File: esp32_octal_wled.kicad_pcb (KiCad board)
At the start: 4 copper layers, 100 x 50 mm, 54 parts, among them J1 LED1, J11 I2C_Display, J12 ATX-24, J13 LED1, J14 LED1, J15 LED1, J16 LED1, J2 LED1, J3 PROG, J4 LED1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

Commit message: As ordered at JLCPCB
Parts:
- R2: value 10k -> 22k
- R3: value 10k -> 15k
- moved SW2 0.85 mm to (136.2, 71.8)
- moved C8 0.75 mm to (126.8, 69.9)
- moved R8 0.75 mm to (126.8, 71.9)
- moved SW4 0.35 mm to (123.2, 71.8)
- moved C9 0.35 mm to (113.8, 69.9)
- moved R12 0.30 mm to (113.9, 71.9)
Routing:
- net GND: track 44.9 -> 57.3 mm, vias 14 -> 118
- net +5V: track 112.7 -> 119.3 mm
- net SDA: track 67.7 -> 73.4 mm
- net 485_DE: track 23.8 -> 22.1 mm
- net Net-(J12-PWR_OK): track 35.9 -> 34.5 mm
- net Net-(R8-Pad1): track 8.54 -> 9.29 mm
- net +3V3: track 119.8 -> 119.3 mm, vias 28 -> 44
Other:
- board text added: "12V"
- board text added: "3V"
- board text added: "485A"
- board text added: "485B"
- board text added: "5V"
- board text added: "GND"
- board text added: "SCL"
- board text added: "SDA"

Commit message: Fixes
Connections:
- U2 pad 29: STRIP3 -> STRIP4
- U2 pad 30: STRIP4 -> STRIP3
- U2 pad 31: STRIP1 -> STRIP2
- U2 pad 33: STRIP2 -> STRIP1
- U3 pad 12: STRIP4 -> STRIP3
- U3 pad 2: STRIP1 -> STRIP2
- U3 pad 5: STRIP2 -> STRIP1
- U3 pad 9: STRIP3 -> STRIP4
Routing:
- net STRIP4: track 18.9 -> 12.7 mm
- net STRIP3: track 12.7 -> 18.9 mm
- net STRIP2: track 20.4 -> 21.4 mm
- net STRIP1: track 21.4 -> 20.4 mm
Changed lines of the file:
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@@
 			(layers "F.Cu" "F.Paste" "F.Mask")
 			(roundrect_rratio 0.25)
-			(net 29 "STRIP1")
+			(net 27 "STRIP2")
 			(pintype "input")
 		)
@@
 			(layers "F.Cu" "F.Paste" "F.Mask")
 			(roundrect_rratio 0.25)
-			(net 27 "STRIP2")
+			(net 29 "STRIP1")
 			(pintype "input")
 		)
@@
 			(layers "F.Cu" "F.Paste" "F.Mask")
 			(roundrect_rratio 0.25)
-			(net 28 "STRIP3")
+			(net 30 "STRIP4")
 			(pintype "input")
 		)
@@
 			(layers "F.Cu" "F.Paste" "F.Mask")
 			(roundrect_rratio 0.25)
-			(net 30 "STRIP4")
+			(net 28 "STRIP3")
 			(pintype "input")
 		)
@@
 			(layers "F.Cu" "F.Paste" "F.Mask")
 			(roundrect_rratio 0.25)
-			(net 28 "STRIP3")
+			(net 30 "STRIP4")
 			(pinfunction "GPIO5")
 			(pintype "bidirectional")
@@
 			(layers "F.Cu" "F.Paste" "F.Mask")
 			(roundrect_rratio 0.25)
-			(net 30 "STRIP4")
+			(net 28 "STRIP3")
 			(pinfunction "GPIO18")
 			(pintype "bidirectional")
@@
 			(layers "F.Cu" "F.Paste" "F.Mask")
 			(roundrect_rratio 0.25)
-			(net 29 "STRIP1")
+			(net 27 "STRIP2")
 			(pinfunction "GPIO19")
 			(pintype "bidirectional")
@@
 			(layers "F.Cu" "F.Paste" "F.Mask")
 			(roundrect_rratio 0.25)
-			(net 27 "STRIP2")
+			(net 29 "STRIP1")
 			(pinfunction "GPIO21")
 			(pintype "bidirectional")
@@
 	)
 	(segment
-		(start 61.812107 60)
-		(end 60.007106 60)
+		(start 77.04 58.224999)
+		(end 75.364999 59.9)
 		(width 0.3)
 		(layer "F.Cu")
@@
 	)
 	(segment
-		(start 62.412106 59.4)
-		(end 62.105 59.707106)
+		(start 75.364999 59.9)
+		(end 63.19 59.9)
 		(width 0.3)
 		(layer "F.Cu")
@@
 	)
 	(segment
-		(start 62.105 59.707107)
-		(end 61.812107 60)
+		(start 60.19 62.9)
+		(end 60.19 64.4)
 		(width 0.3)
 		(layer "F.Cu")
@@
 	)
 	(segment
-		(start 72.054999 59.4)
-		(end 62.412106 59.4)
+		(start 63.19 59.9)
+		(end 60.19 62.9)
 		(width 0.3)
 		(layer "F.Cu")
@@
 	)
 	(segment
-		(start 60.007106 60)
-		(end 57.65 62.357106)
+		(start 77.04 57.125)
+		(end 77.04 58.224999)
 		(width 0.3)
 		(layer "F.Cu")
@@
 	)
 	(segment
-		(start 62.105 59.707106)
-		(end 62.105 59.707107)
+		(start 75.938554 61.877893)
+		(end 75.938553 62.306447)
 		(width 0.3)
 		(layer "F.Cu")
-		(net 27)
+		(net 28)
 	)
 	(segment
-		(start 73.23 58.224999)
-		(end 72.054999 59.4)
+		(start 63.5 60.4)
+		(end 61.46 62.44)
 		(width 0.3)
 		(layer "F.Cu")
-		(net 27)
+		(net 28)
 	)
 	(segment
-		(start 73.23 57.125)
-		(end 73.23 58.224999)
+		(start 75.77 62.475)
+		(end 75.77 61.709339)
 		(width 0.3)
 		(layer "F.Cu")
-		(net 27)
+		(net 28)
 	)
 	(segment
-		(start 57.65 62.357106)
-		(end 57.65 64.4)
+		(start 61.46 62.44)
+		(end 61.46 64.4)
 		(width 0.3)
 		(layer "F.Cu")
-		(net 27)
+		(net 28)
 	)
 	(segment
-		(start 72.128554 62.102292)
-		(end 70.926262 60.9)
+		(start 74.460661 60.4)
+		(end 63.5 60.4)
 		(width 0.3)
 		(layer "F.Cu")
@@
 	)
 	(segment
-		(start 70.926262 60.9)
-		(end 64.240592 60.9)
+		(start 75.77 61.709339)
+		(end 74.460661 60.4)
 		(width 0.3)
 		(layer "F.Cu")
@@
 	)
 	(segment
-		(start 62.73 62.410592)
-		(end 62.73 64.4)
+		(start 61.812107 60)
+		(end 60.007106 60)
 		(width 0.3)
 		(layer "F.Cu")
-		(net 28)
+		(net 29)
 	)
 	(segment
-		(start 72.128553 62.306447)
-		(end 72.128554 62.102292)
+		(start 62.412106 59.4)
+		(end 62.105 59.707106)
 		(width 0.3)
 		(layer "F.Cu")
-		(net 28)
+		(net 29)
 	)
 	(segment
-		(start 64.240592 60.9)
-		(end 62.73 62.410592)
+		(start 62.105 59.707107)
+		(end 61.812107 60)
 		(width 0.3)
 		(layer "F.Cu")
-		(net 28)
+		(net 29)
 	)
 	(segment
-		(start 77.04 58.224999)
-		(end 75.364999 59.9)
+		(start 72.054999 59.4)
+		(end 62.412106 59.4)
 		(width 0.3)
 		(layer "F.Cu")
@@
 	)
 	(segment
-		(start 75.364999 59.9)
-		(end 63.19 59.9)
+		(start 60.007106 60)
+		(end 57.65 62.357106)
 		(width 0.3)
 		(layer "F.Cu")
@@
 	)
 	(segment
-		(start 60.19 62.9)
-		(end 60.19 64.4)
+		(start 62.105 59.707106)
+		(end 62.105 59.707107)
 		(width 0.3)
 		(layer "F.Cu")
@@
 	)
 	(segment
-		(start 63.19 59.9)
-		(end 60.19 62.9)
+		(start 73.23 58.224999)
+		(end 72.054999 59.4)
 		(width 0.3)
 		(layer "F.Cu")
@@
 	)
 	(segment
-		(start 77.04 57.125)
-		(end 77.04 58.224999)
+		(start 73.23 57.125)
+		(end 73.23 58.224999)
 		(width 0.3)
 		(layer "F.Cu")
@@
 	)
 	(segment
-		(start 75.938554 61.877893)
-		(end 75.938553 62.306447)
+		(start 57.65 62.357106)
+		(end 57.65 64.4)
 		(width 0.3)
 		(layer "F.Cu")
-		(net 30)
+		(net 29)
 	)
 	(segment
-		(start 63.5 60.4)
-		(end 61.46 62.44)
+		(start 72.128554 62.102292)
+		(end 70.926262 60.9)
 		(width 0.3)
 		(layer "F.Cu")
@@
 	)
 	(segment
-		(start 75.77 62.475)
-		(end 75.77 61.709339)
+		(start 70.926262 60.9)
+		(end 64.240592 60.9)
 		(width 0.3)
 		(layer "F.Cu")
@@
 	)
 	(segment
-		(start 61.46 62.44)
-		(end 61.46 64.4)
+		(start 62.73 62.410592)
+		(end 62.73 64.4)
 		(width 0.3)
 		(layer "F.Cu")
@@
 	)
 	(segment
-		(start 74.460661 60.4)
-		(end 63.5 60.4)
+		(start 72.128553 62.306447)
+		(end 72.128554 62.102292)
 		(width 0.3)
 		(layer "F.Cu")
@@
 	)
 	(segment
-		(start 75.77 61.709339)
-		(end 74.460661 60.4)
+		(start 64.240592 60.9)
+		(end 62.73 62.410592)
 		(width 0.3)
 		(layer "F.Cu")

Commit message: INMP441
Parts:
- added F1: 2A, Fuse:Fuse_2920_7451Metric_Pad2.10x5.45mm_HandSolder, B.Cu at (58.0, 48.1)
- added F2: 2A, Fuse:Fuse_2920_7451Metric_Pad2.10x5.45mm_HandSolder, B.Cu at (70.0, 48.1)
- added F3: 2A, Fuse:Fuse_2920_7451Metric_Pad2.10x5.45mm_HandSolder, B.Cu at (82.0, 48.1)
- added F4: 2A, Fuse:Fuse_2920_7451Metric_Pad2.10x5.45mm_HandSolder, B.Cu at (94.0, 48.1)
- added F5: 2A, Fuse:Fuse_2920_7451Metric_Pad2.10x5.45mm_HandSolder, B.Cu at (106.0, 48.1)
- added F6: 2A, Fuse:Fuse_2920_7451Metric_Pad2.10x5.45mm_HandSolder, B.Cu at (118.0, 48.1)
- added F7: 2A, Fuse:Fuse_2920_7451Metric_Pad2.10x5.45mm_HandSolder, B.Cu at (130.1, 48.1)
- added F8: 2A, Fuse:Fuse_2920_7451Metric_Pad2.10x5.45mm_HandSolder, B.Cu at (142.0, 48.1)
- added J10: EXT2, Connector_JST:JST_XH_B5B-XH-A_1x05_P2.50mm_Vertical, F.Cu at (147.5, 76.7)
- added J9: TXRX, TestPoint:TestPoint_2Pads_Pitch2.54mm_Drill0.8mm, F.Cu at (68.8, 57.9)
- added U6: INMP441_Module, liebler_MODULES:INMP441_Module, F.Cu at (62.6, 86.4)
- J3: footprint liebler_CONN:IDC_2x03_P1.27mm_Vertical -> Connector:Tag-Connect_TC2030-IDC-NL_2x03_P1.27mm_Vertical
- moved R2 3.52 mm to (61.7, 86.9)
- moved R3 3.47 mm to (61.7, 85.0)
- moved R4 2.05 mm to (69.3, 83.6), turned to -90 degrees
- moved R11 1.71 mm to (66.5, 55.8), turned to 0 degrees
- moved C6 1.60 mm to (52.0, 83.3)
- moved C7 1.60 mm to (52.0, 85.3)
- moved U2 1.60 mm to (59.5, 71.8)
- moved R7 1.38 mm to (54.9, 84.5)
- moved C11 1.12 mm to (80.3, 60.7)
- moved J3 1.05 mm to (61.1, 56.6), turned to 0 degrees
- moved U3 0.40 mm to (74.7, 59.5)
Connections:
- J1 pad 1: +12V -> Net-(J1-Pin_1)
- J13 pad 1: +12V -> Net-(J13-Pin_1)
- J14 pad 1: +12V -> Net-(J14-Pin_1)
- J15 pad 1: +12V -> Net-(J15-Pin_1)
- J16 pad 1: +12V -> Net-(J16-Pin_1)
- J2 pad 1: +12V -> Net-(J2-Pin_1)
- J6 pad 1: +12V -> Net-(J6-Pin_1)
- J7 pad 1: +12V -> Net-(J7-Pin_1)
- U2 pad 4: unconnected-(U2-SENSOR_VP/GPIO36/ADC1_CH0-Pad4) -> THERM
- U2 pad 6: PWR_OK -> I2S_SD
- U2 pad 7: THERM -> PWR_OK
- U2 pad 8: unconnected-(U2-32K_XP/GPIO32/ADC1_CH4-Pad8) -> I2S_WS
- U2 pad 9: unconnected-(U2-32K_XN/GPIO33/ADC1_CH5-Pad9) -> I2S_SCK
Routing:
- net +3V3: track 119.3 -> 220.1 mm, vias 44 -> 45
- net SCL2: track 10.4 -> 102.5 mm
- net SDA2: track 11.0 -> 101.2 mm
- net +5V: track 119.3 -> 155.4 mm
- net I2S_WS: track 0.00 -> 9.47 mm
- net PROG_TX: track 10.1 -> 18.6 mm, vias 0 -> 1
- net I2S_SCK: track 0.00 -> 7.15 mm
- net THERM: track 74.3 -> 80.2 mm
- net Net-(J2-Pin_1): track 0.00 -> 5.01 mm
- net Net-(J15-Pin_1): track 0.00 -> 4.93 mm
- net Net-(J7-Pin_1): track 0.00 -> 4.91 mm
- net Net-(J6-Pin_1): track 0.00 -> 4.91 mm
- net Net-(J16-Pin_1): track 0.00 -> 4.91 mm
- net Net-(J14-Pin_1): track 0.00 -> 4.91 mm
- net Net-(J13-Pin_1): track 0.00 -> 4.91 mm
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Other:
- board text added: "RXTX"
- board text removed: "RS485"

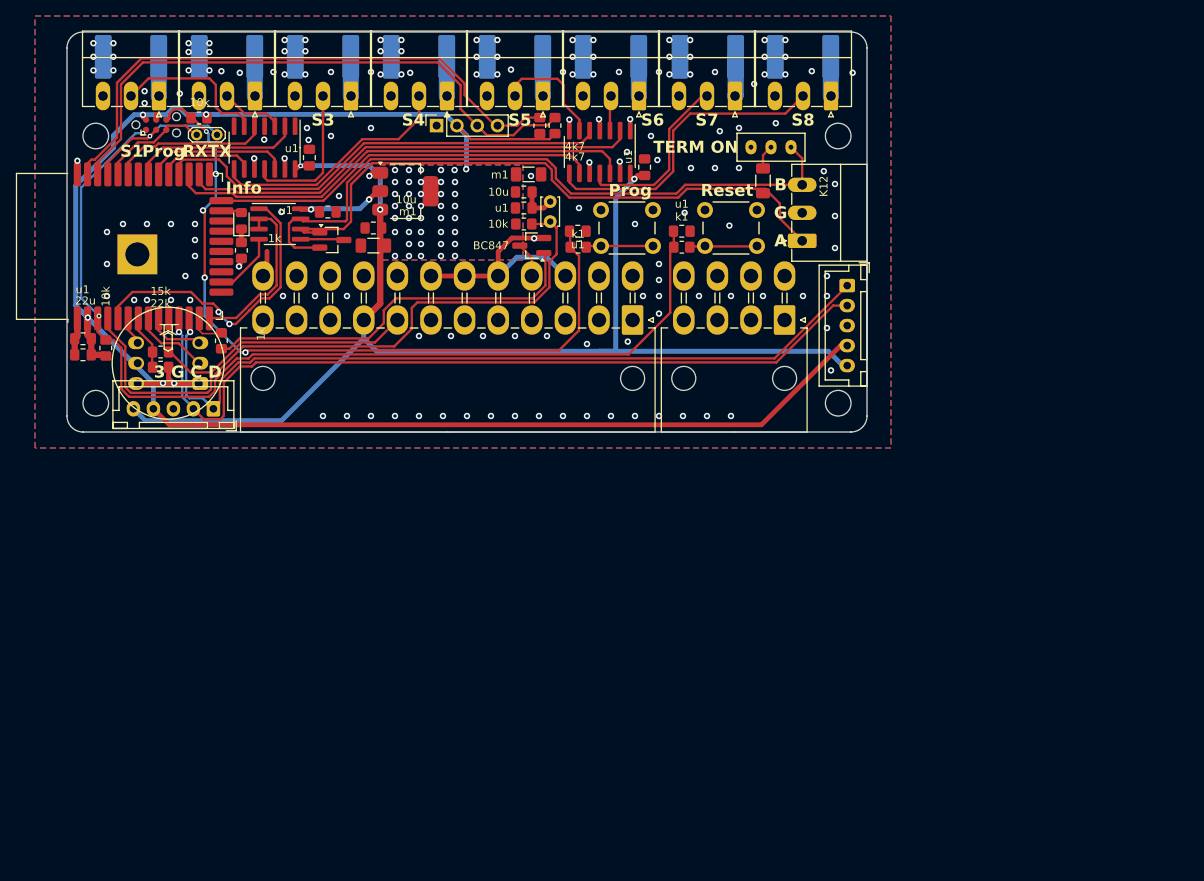
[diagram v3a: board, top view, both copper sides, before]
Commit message: Two layer PCB, other PCB format
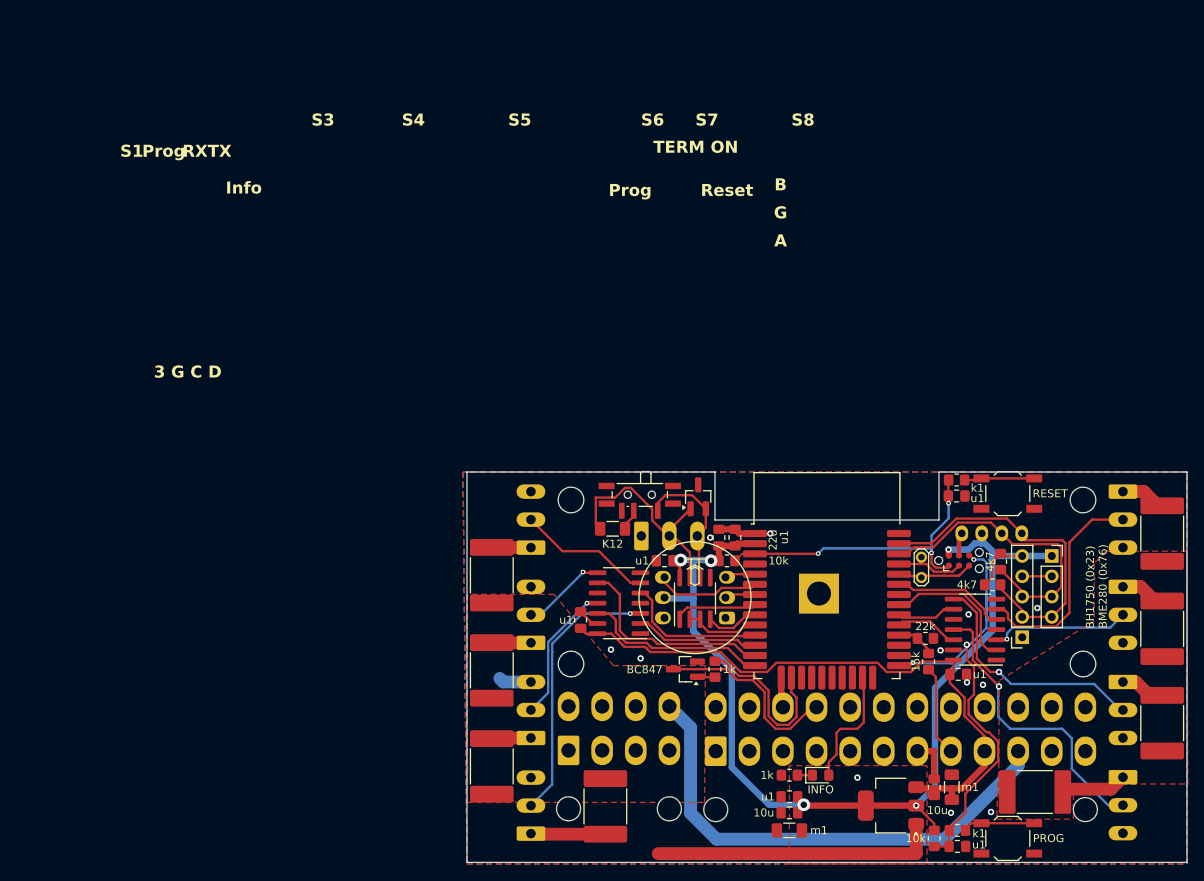
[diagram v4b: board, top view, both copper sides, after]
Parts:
- removed J10, J5: EXT2, Connector_JST:JST_XH_B5B-XH-A_1x05_P2.50mm_Vertical
- removed R13: 10k, Resistor_SMD:R_0805_2012Metric_Pad1.20x1.40mm_HandSolder
- removed TH1: NTC, Capacitor_THT:C_Disc_D3.4mm_W2.1mm_P2.50mm
- added J17: BH1750 (0x23), Connector_PinSocket_2.54mm:PinSocket_1x05_P2.54mm_Vertical, F.Cu at (169.4, 120.7)
- added J18: BME280 (0x76), Connector_PinSocket_2.54mm:PinSocket_1x04_P2.54mm_Vertical, F.Cu at (173.1, 110.5)
- F1, F2, F3, F4, F5, F6, F7, F8: moved to F.Cu
- J1, J12, J13, J14, J15, J16, J2, J4, J6, J7, J8: moved to B.Cu
- J11: value I2C_Display -> I2C EXT; footprint Connector_PinSocket_2.54mm:PinSocket_1x04_P2.54mm_Vertical -> liebler_CONN:JST_XH_S4B-XH-A-1_1x04_P2.50mm_Horizontal_SmallerCourtyard; moved to B.Cu
- SW1: footprint liebler_MECH:Switch_SS12D00 -> liebler_MECH:SW_SPDT_PCM12_handsolder
- SW2, SW4: footprint Button_Switch_THT:SW_PUSH_6mm_H13mm -> liebler_MECH:SW_SPST_TL3342_smaller_handsolder
- moved R11 128.7 mm to (158.4, 145.8), turned to 90 degrees
- moved J3 114.2 mm to (161.5, 111.1)
- moved F1 110.9 mm to (117.3, 141.8), turned to -90 degrees
- moved C11 103.7 mm to (161.4, 125.3), turned to 0 degrees
- moved R3 103.5 mm to (157.7, 123.7), turned to -90 degrees
- moved J9 102.7 mm to (156.8, 110.7), turned to -90 degrees
- moved J1 101.8 mm to (108.0, 141.7), turned to 90 degrees
- moved R2 101.4 mm to (157.3, 120.8)
- moved F7 100.8 mm to (186.9, 131.4), turned to 90 degrees
- moved F5 100.5 mm to (186.9, 107.7), turned to 90 degrees
- moved D2 100.2 mm to (144.2, 137.9), turned to 0 degrees
- moved F6 99.3 mm to (186.9, 119.6), turned to 90 degrees
- moved C1 99.0 mm to (160.6, 139.4), turned to 90 degrees
- moved C2 99.0 mm to (158.4, 139.4), turned to 90 degrees
- moved U1 97.9 mm to (153.0, 141.7), turned to 180 degrees
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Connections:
- D1 pad 1: RS485A -> RS485B
- D1 pad 2: RS485B -> RS485A
- J4 pad 1: RS485A -> GND
- J4 pad 2: GND -> RS485B
- J4 pad 3: RS485B -> RS485A
- R1 pad 1: RS485A -> RS485B
- SW1 pad 1: RS485B -> RS485A
- U2 pad 10: unconnected-(U2-DAC_1/ADC2_CH8/GPIO25-Pad10) -> 485_DE
- U2 pad 11: SCL2 -> STRIP4
- U2 pad 12: SDA2 -> STRIP1
- U2 pad 13: K1 -> STRIP3
- U2 pad 14: 485_DE -> STRIP2
- U2 pad 16: 485_DI -> K1
- U2 pad 24: STRIP8 -> unconnected-(U2-ADC2_CH2/GPIO2-Pad24)
- U2 pad 26: STRIP6 -> unconnected-(U2-ADC2_CH0/GPIO4-Pad26)
- U2 pad 27: STRIP7 -> unconnected-(U2-GPIO16-Pad27)
- U2 pad 28: STRIP5 -> PWR_OK
- U2 pad 29: STRIP4 -> STRIP8
- U2 pad 30: STRIP3 -> STRIP7
- U2 pad 31: STRIP2 -> STRIP6
- U2 pad 33: STRIP1 -> STRIP5
- U2 pad 5: 485_RO -> I2S_SCK
- U2 pad 7: PWR_OK -> I2S_WS
- U2 pad 8: I2S_WS -> 485_RO
- U2 pad 9: I2S_SCK -> 485_DI
- U3 pad 11: STRIP_5V_3 -> STRIP_5V_2
- U3 pad 12: STRIP3 -> STRIP2
- U3 pad 2: STRIP2 -> STRIP1
- U3 pad 3: STRIP_5V_2 -> STRIP_5V_1
- U3 pad 5: STRIP1 -> STRIP4
- U3 pad 6: STRIP_5V_1 -> STRIP_5V_4
- U3 pad 8: STRIP_5V_4 -> STRIP_5V_3
- U3 pad 9: STRIP4 -> STRIP3
- U4 pad 11: STRIP_5V_7 -> STRIP_5V_8
- U4 pad 12: STRIP7 -> STRIP8
- U4 pad 8: STRIP_5V_8 -> STRIP_5V_7
- U4 pad 9: STRIP8 -> STRIP7
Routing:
- net SCL2: track 102.5 -> 0.00 mm, vias 1 -> 0
- net SDA2: track 101.2 -> 0.00 mm, vias 1 -> 0
- net +3V3: track 220.1 -> 136.3 mm, vias 45 -> 5
- net PROG_EN: track 123.2 -> 39.6 mm, vias 2 -> 3
- net THERM: track 80.2 -> 0.00 mm
- net +5V: track 155.4 -> 77.7 mm, vias 3 -> 0
- net +12V: track 0.00 -> 62.4 mm, vias 48 -> 0
- net RS485A: track 78.2 -> 17.3 mm
- net RS485B: track 84.3 -> 28.2 mm
- net STRIP7: track 59.2 -> 7.41 mm
- net Net-(Q2-B): track 48.6 -> 2.22 mm
- net STRIP5: track 56.5 -> 14.3 mm
- net STRIP8: track 48.7 -> 7.94 mm
- net STRIP6: track 57.0 -> 17.9 mm
- net SCL: track 74.3 -> 38.0 mm
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- added copper zone on F.Cu, net +12V
- removed copper zone on In1.Cu, net +12V
- removed copper zone on B.Cu, net +3V3
- removed copper zone on In2.Cu, net GND
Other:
- board size 100 x 50 mm -> 90 x 48.8 mm
- copper layers 4 -> 2

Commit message: Various
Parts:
- added C13: u1, Capacitor_SMD:C_0805_2012Metric_Pad1.18x1.45mm_HandSolder, F.Cu at (160.0, 118.5)
- added J5: CAN, Connector_Phoenix_MC:PhoenixContact_MCV_1,5_2-G-3.5_1x02_P3.50mm_Vertical, B.Cu at (167.7, 121.3)
- added R10: 10k, Resistor_SMD:R_0805_2012Metric_Pad1.20x1.40mm_HandSolder, F.Cu at (166.3, 118.5)
- added R14: 1k, Resistor_SMD:R_0805_2012Metric_Pad1.20x1.40mm_HandSolder, F.Cu at (123.8, 123.7)
- added U10: SR602, liebler_MODULES:PIR_Sensor_SR602, B.Cu at (113.6, 113.5)
- added U7: SN65HVD230, liebler_SEMICONDUCTORS:SOIC-8_3.9x4.9mm_P1.27mm_handsolder, F.Cu at (161.8, 123.2)
- added U9: DS18B20, Package_TO_SOT_THT:TO-92L_HandSolder, B.Cu at (119.8, 123.8)
- J17, J18, U6: moved to B.Cu
- J4: value LED1 -> RS485
- moved R1 14.4 mm to (104.5, 102.7), turned to 90 degrees
- moved J17 13.3 mm to (157.1, 115.7)
- moved U4 11.5 mm to (174.0, 114.9)
- moved C11 10.3 mm to (169.2, 118.5), turned to 90 degrees
- moved R3 8.28 mm to (164.1, 118.5)
- moved C9 7.20 mm to (164.3, 140.2)
- moved U3 7.11 mm to (113.8, 111.5)
- moved R9 6.50 mm to (146.8, 137.8)
- moved J18 6.36 mm to (168.3, 114.7), turned to 90 degrees
- moved D2 6.30 mm to (150.5, 137.8)
- moved C2 6.01 mm to (164.3, 138.2), turned to 0 degrees
- moved R11 5.64 mm to (163.3, 143.1)
- moved R2 5.21 mm to (161.9, 118.5), turned to 90 degrees
- moved U1 5.14 mm to (158.0, 142.9)
- moved R5 4.44 mm to (167.0, 109.8)
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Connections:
- J11 pad 1: GND -> +3V3
- J11 pad 2: +3V3 -> GND
- J4 pad 2: RS485B -> RS485A
- J4 pad 3: RS485A -> RS485B
- SW1 pad CASE: (no net) -> GND
- U2 pad 10: 485_DE -> 485_DI
- U2 pad 16: K1 -> Onewire
- U2 pad 24: unconnected-(U2-ADC2_CH2/GPIO2-Pad24) -> K1
- U2 pad 26: unconnected-(U2-ADC2_CH0/GPIO4-Pad26) -> CAN_RX
- U2 pad 27: unconnected-(U2-GPIO16-Pad27) -> CAN_TX
- U2 pad 4: THERM -> MOVE
- U2 pad 5: I2S_SCK -> I2S_SD
- U2 pad 6: I2S_SD -> 485_RO
- U2 pad 8: 485_RO -> 485_DE
- U2 pad 9: 485_DI -> I2S_SCK
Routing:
- net GND: track 63.4 -> 143.0 mm, vias 12 -> 117
- net +5V: track 77.7 -> 127.5 mm, vias 0 -> 1
- net Onewire: track 0.00 -> 24.5 mm
- net MOVE: track 0.00 -> 19.3 mm
- net STRIP_5V_5: track 27.8 -> 9.26 mm
- net Net-(SW1-B): track 2.70 -> 20.1 mm
- net PWR_OK: track 4.95 -> 18.8 mm, vias 0 -> 2
- net STRIP7: track 7.41 -> 20.9 mm
- net STRIP6: track 17.9 -> 31.4 mm
- net STRIP5: track 14.3 -> 26.1 mm
- net STRIP8: track 7.94 -> 19.5 mm
- net STRIP_5V_6: track 17.5 -> 6.03 mm
- net RS485B: track 28.2 -> 37.9 mm, vias 0 -> 1
- net SCL: track 38.0 -> 47.7 mm, vias 0 -> 1
- net STRIP4: track 18.1 -> 27.2 mm
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- added copper zone on B.Cu, net +3V3
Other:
- board size 90 x 48.8 mm -> 90 x 48.9 mm
- board text added: "1wire"
- board text added: "3"
- board text added: "3V3"
- board text added: "BH1750"
- board text added: "BME280"
- board text added: "C"
- board text added: "CANH"
- board text added: "CANL"
- board text added: "D"
- board text added: "MOVE"
- board text added: "OFF"
- board text added: "ON"
- board text added: "OctaLED v1.0 Klaus Liebler"
- board text added: "RX"
- board text added: "SC"
- board text added: "SD"
- board text added: "Strip 1"
- board text added: "Strip 2"
- board text added: "Strip 3"
- board text added: "Strip 4"
- board text added: "Strip 5"
- board text added: "Strip 6"
- board text added: "Strip 7"
- board text added: "Strip 8"
- board text added: "TERMIN."
- board text added: "TX"
- board text added: "WS"
- board text removed: "3 G C D"
- board text removed: "3V"
- board text removed: "5V"
- board text removed: "A"
- board text removed: "B"
- board text removed: "Info"
- board text removed: "Prog"
- board text removed: "RXTX"
- board text removed: "Reset"
- board text removed: "TERM ON"

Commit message: OctalWLED as ordered @ JLCPCB
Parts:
- moved R8 3.30 mm to (162.2, 104.2)
- moved R6 3.13 mm to (166.8, 109.5), turned to 0 degrees
- moved R5 1.66 mm to (166.8, 111.5)
- moved C8 1.07 mm to (162.2, 102.0)
- moved C12 0.40 mm to (124.8, 111.1)
- moved J9 0.30 mm to (156.5, 110.3)
- moved U10 0.29 mm to (113.8, 113.7)
- moved U3 0.20 mm to (114.0, 111.5)
- moved C10 0.07 mm to (113.0, 117.2), turned to 180 degrees
- turned SW2 to 180 degrees
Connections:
- J11 pad 1: +3V3 -> GND
- J11 pad 2: GND -> +3V3
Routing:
- net GND: track 143.0 -> 167.2 mm, vias 117 -> 153
- net SDA: track 44.4 -> 51.2 mm
- net SCL: track 47.7 -> 45.4 mm
- net PROG_EN: track 40.2 -> 38.7 mm
- net STRIP_5V_3: track 13.7 -> 12.6 mm
- net +3V3: track 138.0 -> 139.0 mm, vias 27 -> 26
- net STRIP5: track 26.1 -> 27.0 mm
- net PROG_IO0: track 55.9 -> 56.8 mm, vias 3 -> 4
- net +5V: track 127.5 -> 126.7 mm
- net Net-(R8-Pad1): track 8.78 -> 9.30 mm, vias 0 -> 2
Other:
- board text added: "Octal WLED Module"
- board text added: "Octal WLED Module Klaus Liebler 2025-01-14 MIT License"
- board text removed: "OctaLED v1.0 Klaus Liebler"
